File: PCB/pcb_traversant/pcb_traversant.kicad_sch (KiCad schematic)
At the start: 32 parts, among them J1 Conn_01x08_Pin, J2 Conn_01x02_Pin, J3 NEB_21_R, J4 Conn_01x01_Pin, U2 OPA2604AP, U3 OPA541AP

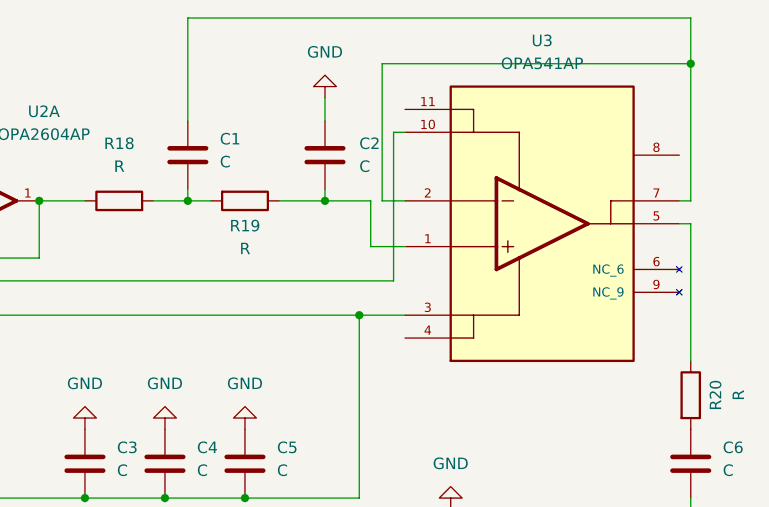
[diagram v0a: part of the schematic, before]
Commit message: Ajout plan de masse et via sur les 2 PCB
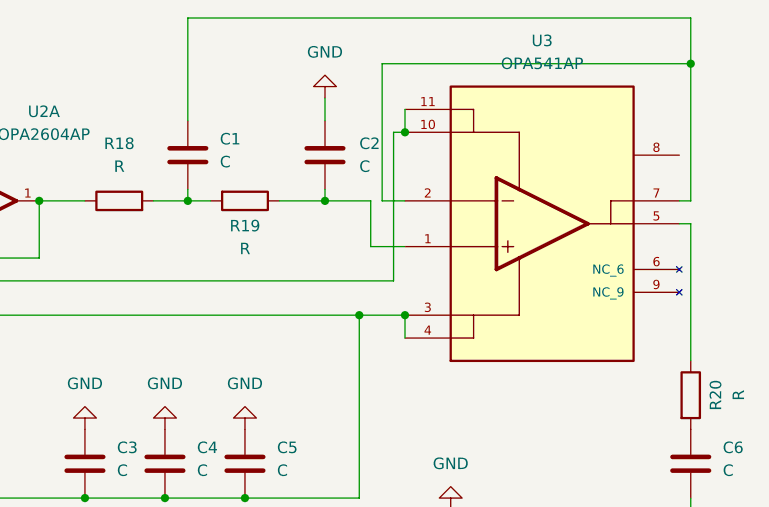
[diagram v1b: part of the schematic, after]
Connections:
- net at C3.2, C4.2, C5.2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: now also U3.4
- net at J4.1 (Pin_1), U2.4, U3.10: now also U3.11
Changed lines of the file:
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@@
+	)
+	(junction
+		(at 231.14 106.68)
+		(diameter 0)
+		(color 0 0 0 0)
 	)
 	(junction
@@
 		(color 0 0 0 0)
 	)
+	(junction
+		(at 231.14 86.36)
+		(diameter 0)
+		(color 0 0 0 0)
+	)
 	(wire
 		(pts
@@
 	(wire
 		(pts
+			(xy 231.14 83.82) (xy 231.14 86.36)
+		)
+		(stroke
+			(width 0)
+			(type default)
+		)
+	)
+	(wire
+		(pts
 			(xy 172.72 106.68) (xy 226.06 106.68)
 		)
@@
 		)
 		(stroke
+			(width 0)
+			(type default)
+		)
+	)
+	(wire
+		(pts
+			(xy 231.14 106.68) (xy 231.14 109.22)
+		)
+		(stroke
